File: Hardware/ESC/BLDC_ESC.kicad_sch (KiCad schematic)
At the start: 1 part, among them J2 Motor Connections

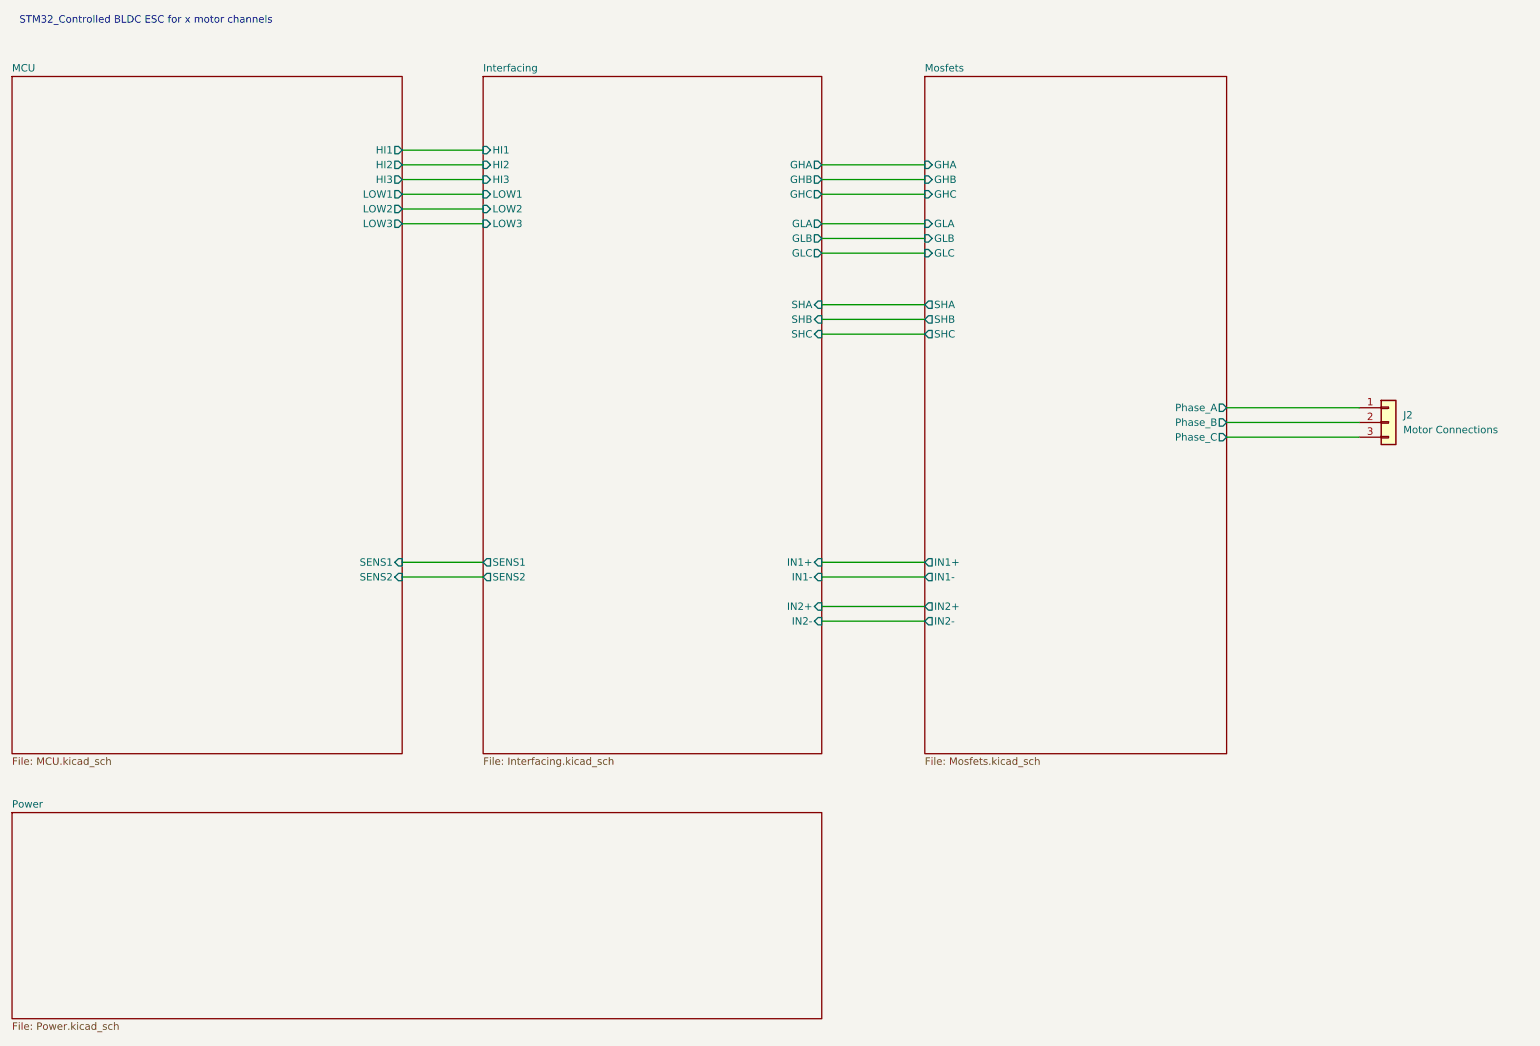
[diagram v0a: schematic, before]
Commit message: Breaking + BEMF ZCD Detector
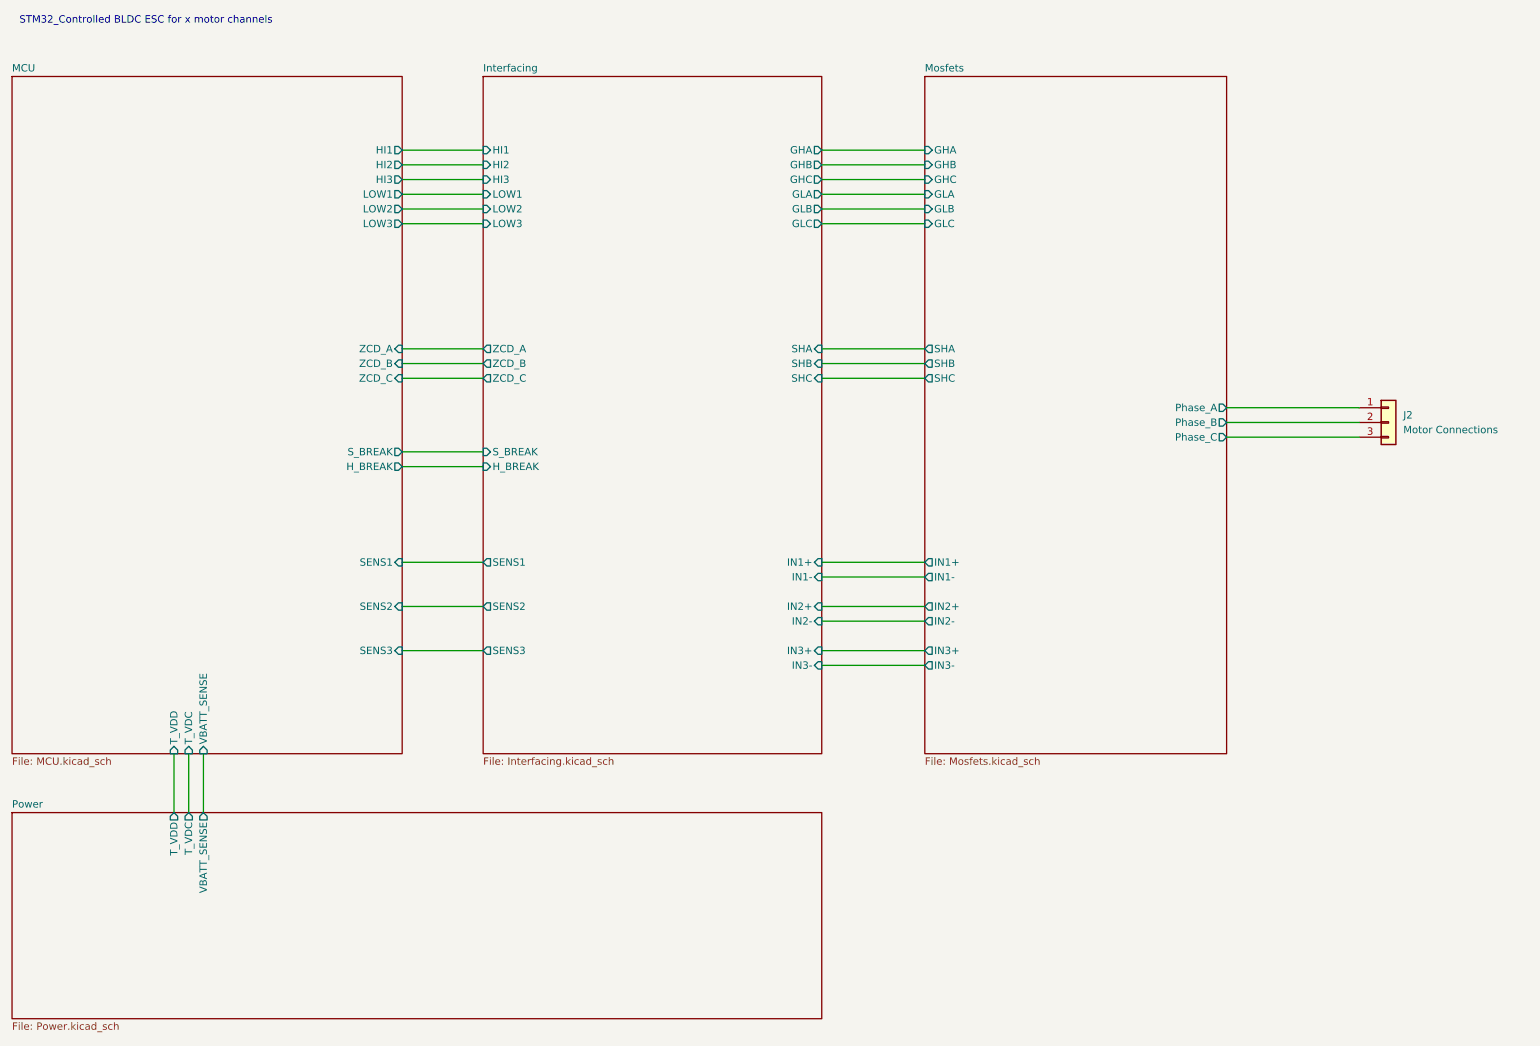
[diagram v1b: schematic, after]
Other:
- sheet Interfacing ports: added H_BREAK, IN3+, IN3-, SENS3, S_BREAK, ZCD_A, ZCD_B, ZCD_C; removed none
- sheet MCU ports: added H_BREAK, SENS3, S_BREAK, T_VDC, T_VDD, VBATT_SENSE, ZCD_A, ZCD_B, ZCD_C; removed none
- sheet Mosfets ports: added IN3+, IN3-; removed none
- sheet Power ports: added T_VDC, T_VDD, VBATT_SENSE; removed none
